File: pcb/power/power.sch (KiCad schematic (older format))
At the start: 9 parts, among them CON1 BARREL_JACK, P1 CONN_01X04, P2 CONN_01X04, P3 CONN_01X04, P4 CONN_01X03, P5 USB_A, P6 CONN_01X03

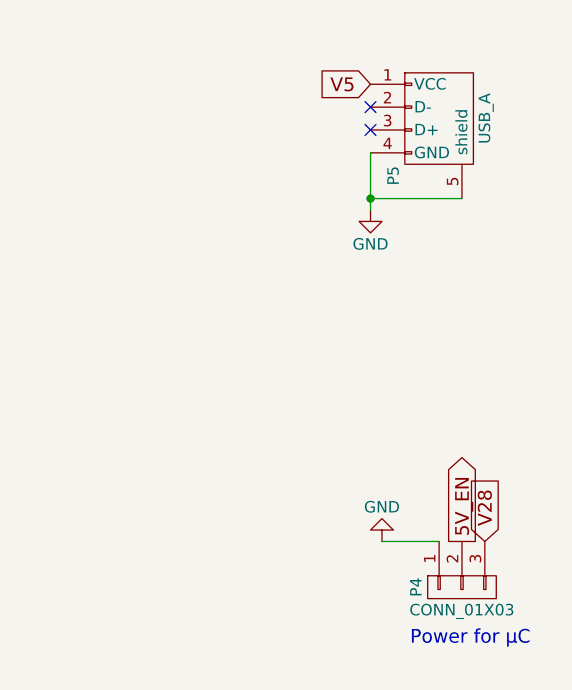
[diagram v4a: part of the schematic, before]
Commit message: Started placing some components.
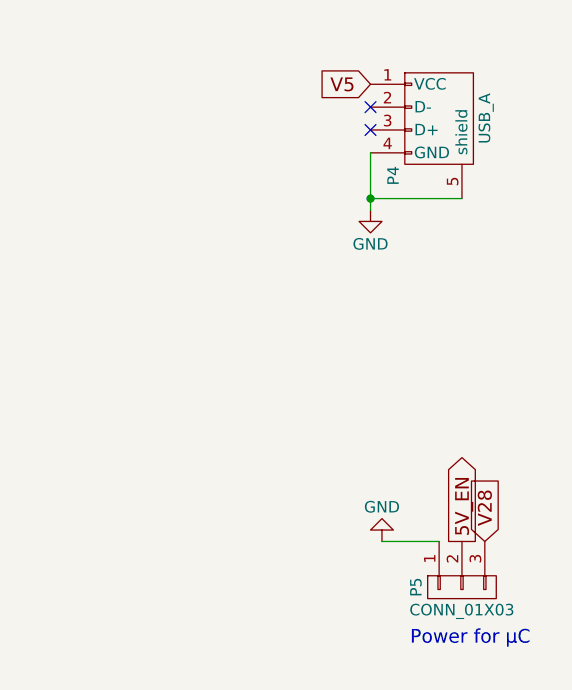
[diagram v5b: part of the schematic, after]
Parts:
- P3: footprint Pin_Headers:Pin_Header_Straight_1x04 -> Additional:LED_CONN_1.25_PITCH
- renumbered P5 to P4, P4 to P5
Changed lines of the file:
@@
 NoConn ~ 9750 3450
 $Comp
-L USB_A P5
+L USB_A P4
 U 1 1 584373B8
 P 10050 3450
-F 0 "P5" H 10250 3250 50  0000 C CNN
+F 0 "P4" H 10250 3250 50  0000 C CNN
 F 1 "USB_A" H 10000 3650 50  0000 C CNN
 F 2 "Connect:USB_A" V 10000 3350 50  0001 C CNN
@@
 Power for µC\n
 $Comp
-L CONN_01X03 P4
+L CONN_01X03 P5
 U 1 1 584384F7
 P 10150 5450
-F 0 "P4" H 10150 5650 50  0000 C CNN
+F 0 "P5" H 10150 5650 50  0000 C CNN
 F 1 "CONN_01X03" V 10250 5450 50  0000 C CNN
 F 2 "Pin_Headers:Pin_Header_Straight_1x03" H 10150 5450 50  0001 C CNN
@@
 F 0 "P3" H 3300 1650 50  0000 C CNN
 F 1 "CONN_01X04" V 3400 1400 50  0000 C CNN
-F 2 "Pin_Headers:Pin_Header_Straight_1x04" H 3300 1400 50  0001 C CNN
+F 2 "Additional:LED_CONN_1.25_PITCH" H 3300 1400 50  0001 C CNN
 F 3 "http://www.sullinscorp.com/drawings/78_P(N)PxCxxxLFBN-RC,_10492-H.pdf" H 3300 1400 50  0001 C CNN
 F 4 "S7002-ND " H 3300 1400 60  0001 C CNN "Digikey"

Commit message: Did a lot of stuff. Currently working on the exact 3D models for the headers.
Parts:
- P1: footprint Pin_Headers:Pin_Header_Straight_1x04 -> Additional:ESQ-104-12-G-S-LL; Digikey S7002-ND -> (none); Samtec (none) -> ESQ-104-12-G-S-LL
- P3: footprint Additional:LED_CONN_1.25_PITCH -> Additional:ESQ-104-12-G-S-LL; Digikey S7002-ND -> (none); Samtec (none) -> ESQ-104-12-G-S-LL
- R1: footprint Resistors_SMD:R_0603_HandSoldering -> Additional:R_0603_HandSoldering_Same_As_C
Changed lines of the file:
@@
 F 0 "P1" H 1250 1650 50  0000 C CNN
 F 1 "CONN_01X04" V 1350 1400 50  0000 C CNN
-F 2 "Pin_Headers:Pin_Header_Straight_1x04" H 1250 1400 50  0001 C CNN
-F 3 "http://www.sullinscorp.com/drawings/78_P(N)PxCxxxLFBN-RC,_10492-H.pdf" H 1250 1400 50  0001 C CNN
-F 4 "S7002-ND " H 1250 1400 60  0001 C CNN "Digikey"
+F 2 "Additional:ESQ-104-12-G-S-LL" H 1250 1400 50  0001 C CNN
+F 3 "https://www.samtec.com/products/esq" H 1250 1400 50  0001 C CNN
+F 4 "ESQ-104-12-G-S-LL" H 1250 1400 60  0001 C CNN "Samtec"
 	1    1250 1400
 	0    -1   -1   0
@@
 F 0 "R1" V 2380 4100 50  0000 C CNN
 F 1 "10k" V 2300 4100 50  0000 C CNN
-F 2 "Resistors_SMD:R_0603_HandSoldering" V 2230 4100 50  0001 C CNN
+F 2 "Additional:R_0603_HandSoldering_Same_As_C" V 2230 4100 50  0001 C CNN
 F 3 "http://www.yageo.com.tw/exep/pages/download/literatures/PYu-R_INT-thick_7.pdf" H 2300 4100 50  0001 C CNN
 F 4 " 311-10.0KHRCT-ND" V 2300 4100 60  0001 C CNN "Digikey"
@@
 F 0 "P3" H 3300 1650 50  0000 C CNN
 F 1 "CONN_01X04" V 3400 1400 50  0000 C CNN
-F 2 "Additional:LED_CONN_1.25_PITCH" H 3300 1400 50  0001 C CNN
-F 3 "http://www.sullinscorp.com/drawings/78_P(N)PxCxxxLFBN-RC,_10492-H.pdf" H 3300 1400 50  0001 C CNN
-F 4 "S7002-ND " H 3300 1400 60  0001 C CNN "Digikey"
+F 2 "Additional:ESQ-104-12-G-S-LL" H 3300 1400 50  0001 C CNN
+F 3 "https://www.samtec.com/products/esq" H 3300 1400 50  0001 C CNN
+F 4 "ESQ-104-12-G-S-LL" H 3300 1400 60  0001 C CNN "Samtec"
 	1    3300 1400
 	0    -1   -1   0

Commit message: Almost finished routing.
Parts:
- P2: footprint Pin_Headers:Pin_Header_Straight_1x04 -> Additional:ESQ-104-12-G-S-LL; Digikey S7002-ND -> (none); Samtec (none) -> ESQ-104-12-G-S-LL
- P3: footprint Additional:ESQ-104-12-G-S-LL -> Additional:LED_CONN_1.25_PITCH; Samtec ESQ-104-12-G-S-LL -> (none)
- P5, P6: footprint Pin_Headers:Pin_Header_Straight_1x03 -> Additional:ESQ-103-12-G-S-LL; Digikey S7036-ND -> (none); Samtec (none) -> ESQ-103-12-G-S-LL
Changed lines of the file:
@@
 F 0 "P2" H 1250 5800 50  0000 C CNN
 F 1 "CONN_01X04" V 1350 5550 50  0000 C CNN
-F 2 "Pin_Headers:Pin_Header_Straight_1x04" H 1250 5550 50  0001 C CNN
-F 3 "http://www.sullinscorp.com/drawings/78_P(N)PxCxxxLFBN-RC,_10492-H.pdf" H 1250 5550 50  0001 C CNN
-F 4 "S7002-ND " H 1250 5550 60  0001 C CNN "Digikey"
+F 2 "Additional:ESQ-104-12-G-S-LL" H 1250 5550 50  0001 C CNN
+F 3 "https://www.samtec.com/products/esq" H 1250 5550 50  0001 C CNN
+F 4 "ESQ-104-12-G-S-LL" H 1250 5550 60  0001 C CNN "Samtec"
 	1    1250 5550
 	0    1    1    0
@@
 F 0 "P6" H 10250 1550 50  0000 C CNN
 F 1 "CONN_01X03" V 10350 1350 50  0000 C CNN
-F 2 "Pin_Headers:Pin_Header_Straight_1x03" H 10250 1350 50  0001 C CNN
-F 3 "http://www.sullinscorp.com/drawings/78_P(N)PxCxxxLFBN-RC,_10492-H.pdf" H 10250 1350 50  0001 C CNN
-F 4 "S7036-ND " H 10250 1350 60  0001 C CNN "Digikey"
+F 2 "Additional:ESQ-103-12-G-S-LL" H 10250 1350 50  0001 C CNN
+F 3 "https://www.samtec.com/products/esq" H 10250 1350 50  0001 C CNN
+F 4 "ESQ-103-12-G-S-LL" H 10250 1350 60  0001 C CNN "Samtec"
 	1    10250 1350
 	0    1    -1   0
@@
 F 0 "P5" H 10150 5650 50  0000 C CNN
 F 1 "CONN_01X03" V 10250 5450 50  0000 C CNN
-F 2 "Pin_Headers:Pin_Header_Straight_1x03" H 10150 5450 50  0001 C CNN
-F 3 "http://www.sullinscorp.com/drawings/78_P(N)PxCxxxLFBN-RC,_10492-H.pdf" H 10150 5450 50  0001 C CNN
-F 4 "S7036-ND " H 10150 5450 60  0001 C CNN "Digikey"
+F 2 "Additional:ESQ-103-12-G-S-LL" H 10150 5450 50  0001 C CNN
+F 3 "https://www.samtec.com/products/esq" H 10150 5450 50  0001 C CNN
+F 4 "ESQ-103-12-G-S-LL" H 10150 5450 60  0001 C CNN "Samtec"
 	1    10150 5450
 	0    -1   1    0
@@
 F 0 "P3" H 3300 1650 50  0000 C CNN
 F 1 "CONN_01X04" V 3400 1400 50  0000 C CNN
-F 2 "Additional:ESQ-104-12-G-S-LL" H 3300 1400 50  0001 C CNN
-F 3 "https://www.samtec.com/products/esq" H 3300 1400 50  0001 C CNN
-F 4 "ESQ-104-12-G-S-LL" H 3300 1400 60  0001 C CNN "Samtec"
+F 2 "Additional:LED_CONN_1.25_PITCH" H 3300 1400 50  0001 C CNN
+F 3 "" H 3300 1400 50  0001 C CNN
 	1    3300 1400
 	0    -1   -1   0

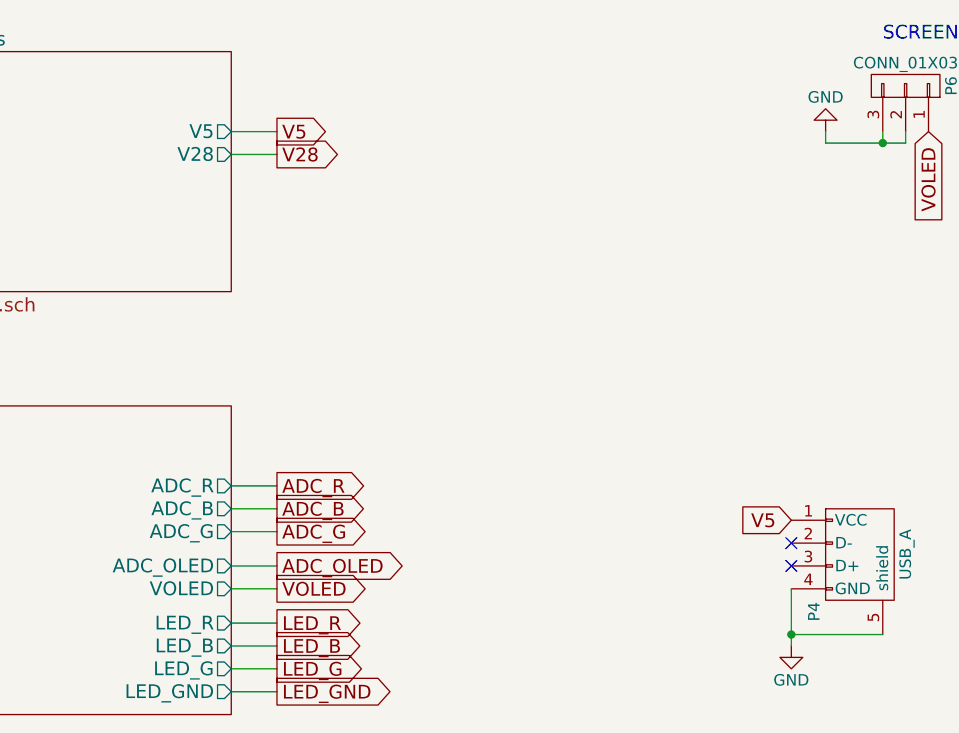
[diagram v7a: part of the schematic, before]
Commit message: Started completely over with the layout, as the OLED would not fit anymore. Also introduced a USB DCP Controller and found a stupid bug in the LED driver.
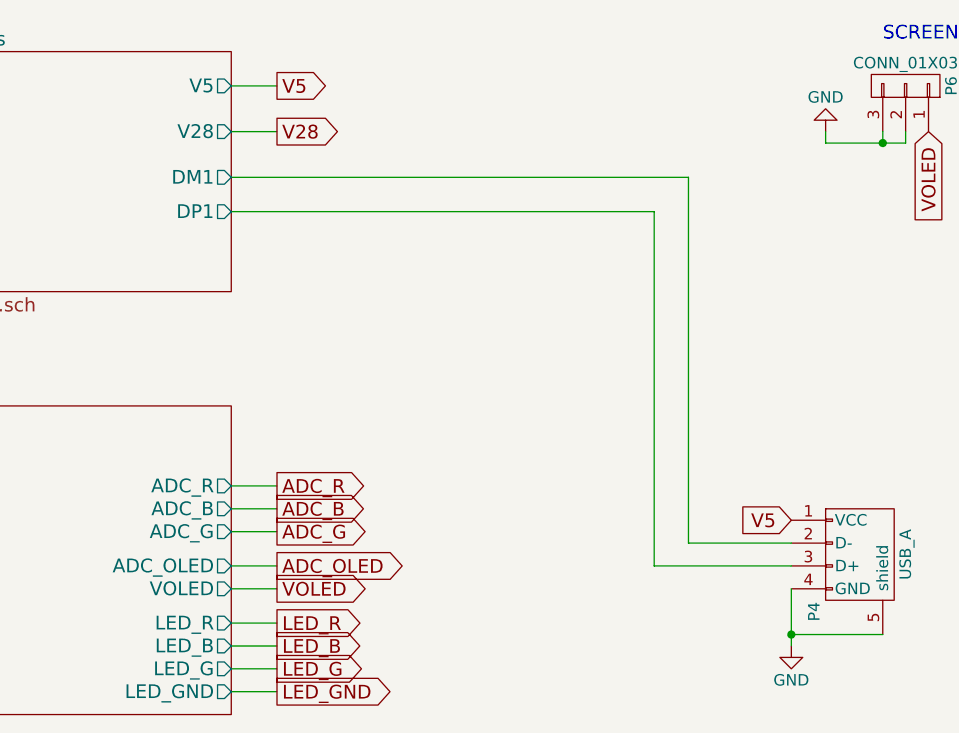
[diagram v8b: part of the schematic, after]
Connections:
- net Bucket Converters/DM1: now reaches P4.2 (D-)
- net Bucket Converters/DP1: now reaches P4.3 (D+)
- no-connect marks 2 -> 0
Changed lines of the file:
@@
 PWM_R
 $Comp
-L GND #PWR01
+L GND #PWR4
 U 1 1 583EB242
 P 9900 1550
-F 0 "#PWR01" H 9900 1300 50  0001 C CNN
+F 0 "#PWR4" H 9900 1300 50  0001 C CNN
 F 1 "GND" H 9900 1400 50  0000 C CNN
 F 2 "" H 9900 1550 50  0000 C CNN
@@
 $EndComp
 $Comp
-L GND #PWR02
+L GND #PWR1
 U 1 1 583C8E04
 P 1650 4350
-F 0 "#PWR02" H 1650 4100 50  0001 C CNN
+F 0 "#PWR1" H 1650 4100 50  0001 C CNN
 F 1 "GND" H 1650 4200 50  0000 C CNN
 F 2 "" H 1650 4350 50  0000 C CNN
@@
 V20
 $Comp
-L PWR_FLAG #FLG03
+L PWR_FLAG #FLG2
 U 1 1 58428672
 P 2300 3350
-F 0 "#FLG03" H 2300 3445 50  0001 C CNN
+F 0 "#FLG2" H 2300 3445 50  0001 C CNN
 F 1 "PWR_FLAG" H 2300 3530 50  0000 C CNN
 F 2 "" H 2300 3350 50  0000 C CNN
@@
 $EndComp
 $Comp
-L PWR_FLAG #FLG04
+L PWR_FLAG #FLG1
 U 1 1 5842A47B
 P 1950 4200
-F 0 "#FLG04" H 1950 4295 50  0001 C CNN
+F 0 "#FLG1" H 1950 4295 50  0001 C CNN
 F 1 "PWR_FLAG" H 1950 4380 50  0000 C CNN
 F 2 "" H 1950 4200 50  0000 C CNN
@@
 F2 "V20" I L 5550 1350 60
 F3 "5V_EN" I L 5550 1550 60
-F4 "V5" O R 7300 1550 60
-F5 "V28" O R 7300 1650 60
+F4 "V5" O R 7300 1350 60
+F5 "V28" O R 7300 1550 60
+F6 "DM1" O R 7300 1750 60
+F7 "DP1" O R 7300 1900 60
 $EndSheet
 $Sheet
@@
 F15 "LED_GND" O R 7300 4000 60
 $EndSheet
-NoConn ~ 9750 3350
-NoConn ~ 9750 3450
 $Comp
 L USB_A P4
@@
 	5400 5500 5550 5500
 $Comp
-L GND #PWR05
+L GND #PWR3
 U 1 1 58444C94
 P 9800 5250
-F 0 "#PWR05" H 9800 5000 50  0001 C CNN
+F 0 "#PWR3" H 9800 5000 50  0001 C CNN
 F 1 "GND" H 9800 5100 50  0000 C CNN
 F 2 "" H 9800 5250 50  0000 C CNN
@@
 Text GLabel 10250 5250 1    60   Input ~ 0
 V28
-Text GLabel 7500 1650 2    60   Output ~ 0
+Text GLabel 7500 1550 2    60   Output ~ 0
 V28
-Wire Wire Line
-	7300 1650 7500 1650
-Text GLabel 7500 1550 2    60   Output ~ 0
+Text GLabel 7500 1350 2    60   Output ~ 0
 V5
-Wire Wire Line
-	7300 1550 7500 1550
 Text GLabel 9750 3250 0    60   Input ~ 0
 V5
 $Comp
-L GND #PWR06
+L GND #PWR2
 U 1 1 58446B04
 P 9750 3800
-F 0 "#PWR06" H 9750 3550 50  0001 C CNN
+F 0 "#PWR2" H 9750 3550 50  0001 C CNN
 F 1 "GND" H 9750 3650 50  0000 C CNN
 F 2 "" H 9750 3800 50  0000 C CNN
@@
 	0    -1   -1   0
 $EndComp
+Wire Wire Line
+	7500 1350 7300 1350
+Wire Wire Line
+	7300 1550 7500 1550
+Wire Wire Line
+	7300 1750 9300 1750
+Wire Wire Line
+	9300 1750 9300 3350
+Wire Wire Line
+	9300 3350 9750 3350
+Wire Wire Line
+	9750 3450 9150 3450
+Wire Wire Line
+	9150 3450 9150 1900
+Wire Wire Line
+	9150 1900 7300 1900
 $EndSCHEMATC
